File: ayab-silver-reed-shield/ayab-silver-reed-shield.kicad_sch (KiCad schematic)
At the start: 16 parts, among them J1 Power, J2 Digital/PWM, J3 Analog, J4 Digital/PWM, J5 DIN-7, J6 Barrel_Jack, K1 Relay_SPST-NO, Q1 2N2222A-TO92

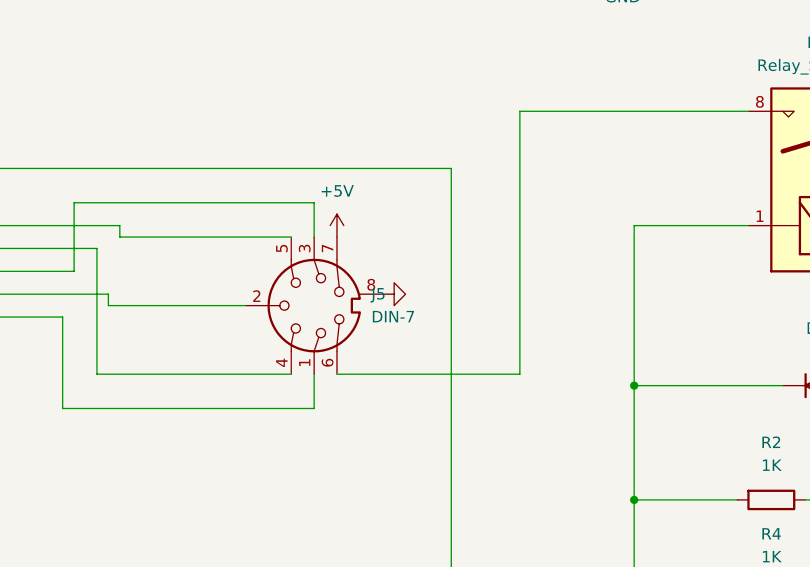
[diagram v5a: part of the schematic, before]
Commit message: feat: add locals symbols
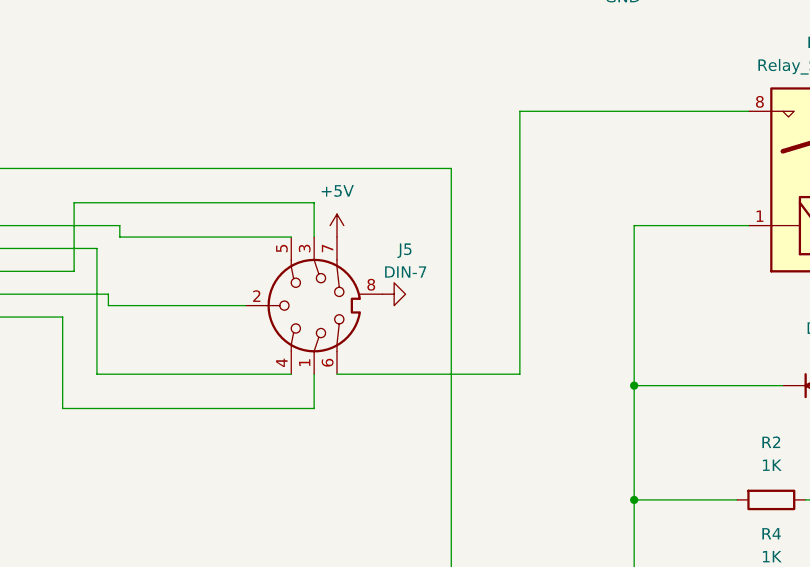
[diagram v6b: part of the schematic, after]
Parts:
- removed J5: DIN-7, Locals:DIN-704-M10, symbol Connector:DIN-7
- removed K1: Relay_SPST-NO, Locals:RELAY_G6DN-1A_OMR, symbol Relay:Relay_SPST-NO
- removed Q1: 2N2222A-TO92, Package_TO_SOT_THT:TO-92_Inline, symbol PCM_Transistor_BJT_AKL:2N2222A-TO92
- added J5: DIN-7, Locals:DIN-704-M10, symbol symbols:DIN-7
- added K1: Relay_SPST-NO, Locals:RELAY_G6DN-1A_OMR, symbol symbols:Relay_SPST-NO
- added Q1: 2N2222A-TO92, Package_TO_SOT_THT:TO-92_Inline, symbol symbols:2N2222A-TO92
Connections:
- net *3: now also J5.2
- net *5: now also J5.4
- net *6: now also J5.5
- net +5V: now also J5.7, K1.1
- net 2: now also J5.1
- net 4: now also J5.3
- net GND: now also J5.8 (GND), Q1.1 (E)
- net at D1.2 (A), D2.1 (K): now also K1.2, Q1.3 (C)
- net at R3.1: now also Q1.2 (B)
- net at C1.2, R1.2: now also K1.5
- new net: J5.6, K1.8

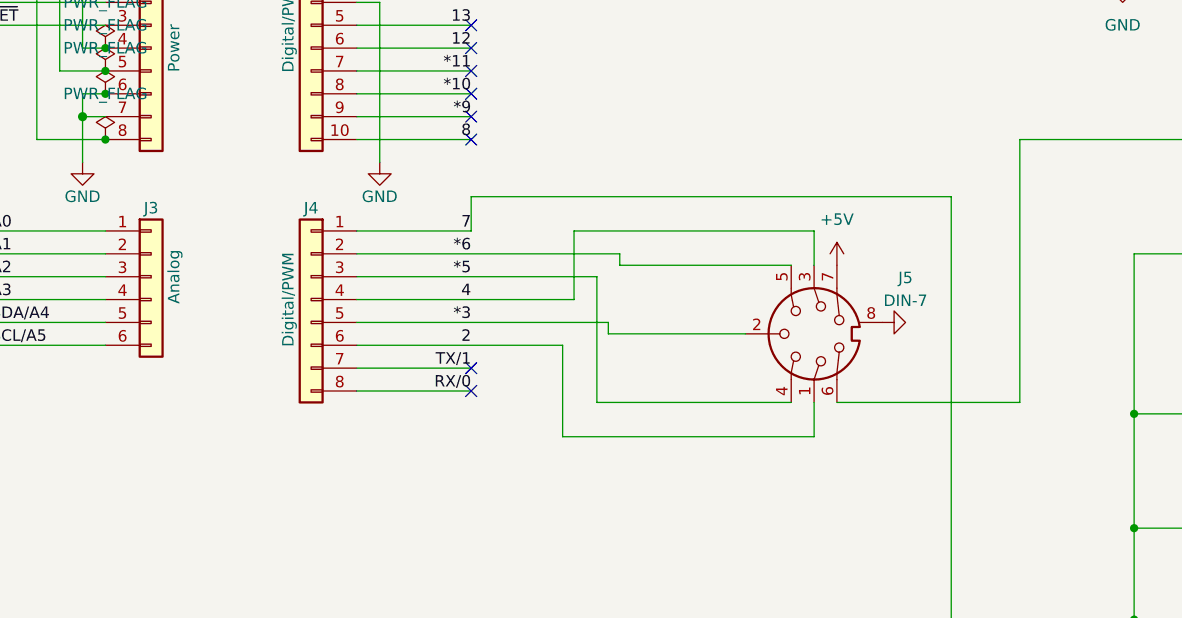
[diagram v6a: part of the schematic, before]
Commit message: feat: new board version with debug
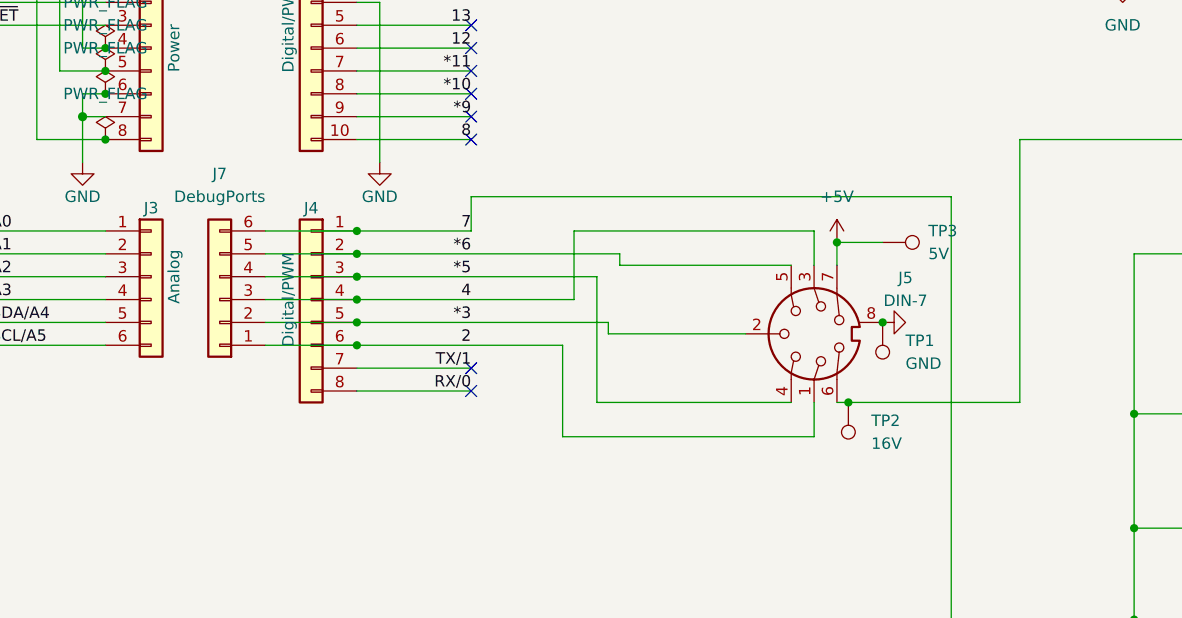
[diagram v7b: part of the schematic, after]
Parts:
- added J7: DebugPorts, Connector_PinHeader_2.54mm:PinHeader_1x06_P2.54mm_Vertical, symbol Connector_Generic:Conn_01x06
- added TP1: GND, TestPoint:TestPoint_Pad_D1.0mm, symbol Connector:TestPoint
- added TP2: 16V, TestPoint:TestPoint_Pad_D1.0mm, symbol Connector:TestPoint
- added TP3: 5V, TestPoint:TestPoint_Pad_D1.0mm, symbol Connector:TestPoint
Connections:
- net *3: now also J7.2 (Pin_2)
- net *5: now also J7.4 (Pin_4)
- net *6: now also J7.5 (Pin_5)
- net +5V: now also TP3.1
- net 2: now also J7.1 (Pin_1)
- net 4: now also J7.3 (Pin_3)
- net 7: now also J7.6 (Pin_6)
- net GND: now also TP1.1
- net at J5.6, K1.8: now also TP2.1

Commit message: wip
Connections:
- net *3 renamed KSL
- net *5 renamed CCP
- net *6 renamed HOK
- net 2: no longer names the net of J4.6 (Pin_6), J7.1 (Pin_1)
- net 2: no longer J5.1
- net 4 renamed DOB
- net 7 renamed SOLENOID_CONTROL
- new net ND1: J5.1
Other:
- moved on the sheet: C1, D1, D2, D3, J5, J6, K1, Q1, R1, R2, R3, R4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
